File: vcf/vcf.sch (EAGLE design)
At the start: 55 parts, among them IC1 OPA4130U, IC2 OPA4130U, IC3 OPA4130U, IC4 OPA4130U, Q1 BC847ASMD, Q2 BC847ASMD, Q3 BC847ASMD, Q4 BC847ASMD, Q5 BC847ASMD, Q6 BC847ASMD

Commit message: lasdkfj
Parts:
- removed U$5: PJ301BM, dan:PJ301BM
- added AIN2, BP, LP: PJ301BM, dan:PJ301BM
- added FREQ, GAIN1, Q: 10K, dan:US-EVUF2J
- added IC5: OPA4130U, dan:OPA4130U
- added R32, R34, R36, R37, R40, R41, R42: 100k, dan:R-US_R0603
- added R33, R35, R38, R39: 1k, dan:R-US_R0603
- added R44: 10k, dan:R-US_R0603
- added X1: 2516-, dan:2516-
- C5, C7: value 1u -> (none); device dan:C-USC0603 -> dan:CPOL-USE2.5-6
- GAIN, MODAMT: value US-EVUF2J -> 10K
- R11, R16, R5: value 1k -> 10k
- R15, R29: value 1k -> 100k
- R17: value US-EVUF2J -> 100k; device dan:US-EVUF2J -> dan:R-US_R0603
- SCALE: value (none) -> 10K
- renumbered R21 to GAIN, R27 to MODAMT, R28 to SCALE, U$4 to AIN, U$6 to MIN, U$7 to MIN2
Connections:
- new net N$48: IC4D.-IN, IC4D.OUT, R35.2
- new net N$49: IC4C.-IN, IC4C.OUT, R33.2
- new net N$50: IC5B.-IN, IC5B.OUT, R38.2
- new net N$51: IC4B.-IN, R32.2, R35.1
- new net N$52: IC4B.OUT, R32.1, R42.2
- new net N$53: IC5C.-IN, IC5C.OUT, R39.2
- new net N$54: IC4B.+IN, R33.1, R34.1
- new net N$55: IC5A.+IN, R37.2, R38.1
- new net N$56: IC5A.-IN, R36.2, R39.1
- new net N$57: BP.P$1, BP.P$2, BP.P$4
- new net N$58: IC5A.OUT, R36.1
- new net N$59: IC5D.-IN, R40.2, R41.1, R42.1
- new net N$60: FREQ.S, R44.1
- new net N$61: BP.P$3, IC5D.OUT, R40.1
- new net N$62: GAIN1.A, R20.1
- net +12V: now also FREQ.E, IC5A.V+, X1-10.KL, X1-9.KL
- net -12V: now also FREQ.A, IC5A.V-, X1-1.KL, X1-2.KL
- net GND: now also AIN2.P$1, AIN2.P$2, AIN2.P$4, IC5D.+IN, LP.P$1, LP.P$2, LP.P$4, R17.2, R34.2, R37.1, X1-3.KL, X1-4.KL, X1-5.KL, X1-6.KL, X1-7.KL, X1-8.KL; no longer U$5.P$1, U$5.P$2, U$5.P$4
- net N$14: now also C5.+; no longer C5.2
- net N$2: now also IC4C.+IN
- net N$21: now also C5.-; no longer C5.1
- net N$27: now also LP.P$3, Q.A; no longer R17.A
- net N$30: now also GAIN1.E, GAIN1.S; no longer R20.1
- net N$31: now also C7.+; no longer C7.1
- net N$32: now also C7.-, Q.E, Q.S; no longer C7.2, R17.E, R17.S
- net N$33: now also AIN2.P$3; no longer U$5.P$3
- net N$36: now also R44.2
- net N$4: now also IC5B.+IN
- net N$45: now also R17.1
- net N$47: now also R41.2
- net N$5: now also IC5C.+IN
- net N$7: now also IC4D.+IN
- net N$8: now also IC1D.+IN; no longer IC1C.+IN
- net N$9: now also IC1C.+IN; no longer IC1D.+IN
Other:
- moved on the sheet: C2, C3, C4, IC1B, IC1C, IC1D, IC2D, IC3C, IC3D, IC4A, IC4B, IC4C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

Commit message: made changes to the vcf board
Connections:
- removed net N$57: BP.P$1, BP.P$2, BP.P$4
- net GND: now also BP.P$1, BP.P$2, BP.P$4, R6.1
- net N$35: now also IC2B.OUT
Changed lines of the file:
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@@
 <wire x1="20.32" y1="10.16" x2="20.32" y2="12.7" width="0.1524" layer="91"/>
 <pinref part="C6" gate="G$1" pin="2"/>
-<wire x1="20.32" y1="12.7" x2="20.32" y2="17.78" width="0.1524" layer="91"/>
+<wire x1="20.32" y1="12.7" x2="20.32" y2="15.24" width="0.1524" layer="91"/>
 <wire x1="7.62" y1="17.78" x2="7.62" y2="12.7" width="0.1524" layer="91"/>
 <wire x1="7.62" y1="12.7" x2="20.32" y2="12.7" width="0.1524" layer="91"/>
 <junction x="20.32" y="12.7"/>
+<pinref part="R6" gate="G$1" pin="1"/>
 </segment>
 <segment>
@@
 <junction x="154.94" y="203.2"/>
 <wire x1="149.86" y1="205.74" x2="154.94" y2="205.74" width="0.1524" layer="91"/>
+<junction x="154.94" y="205.74"/>
+</segment>
+<segment>
+<pinref part="BP" gate="G$1" pin="P$2"/>
+<wire x1="218.44" y1="81.28" x2="215.9" y2="81.28" width="0.1524" layer="91"/>
+<wire x1="215.9" y1="81.28" x2="215.9" y2="86.36" width="0.1524" layer="91"/>
+<pinref part="BP" gate="G$1" pin="P$4"/>
+<wire x1="215.9" y1="86.36" x2="215.9" y2="88.9" width="0.1524" layer="91"/>
+<wire x1="215.9" y1="88.9" x2="218.44" y2="88.9" width="0.1524" layer="91"/>
+<pinref part="BP" gate="G$1" pin="P$1"/>
+<wire x1="218.44" y1="86.36" x2="215.9" y2="86.36" width="0.1524" layer="91"/>
+<junction x="215.9" y="86.36"/>
+<wire x1="215.9" y1="88.9" x2="210.82" y2="88.9" width="0.1524" layer="91"/>
+<wire x1="210.82" y1="88.9" x2="210.82" y2="86.36" width="0.1524" layer="91"/>
+<junction x="215.9" y="88.9"/>
+<pinref part="GND20" gate="1" pin="GND"/>
 </segment>
 </net>
@@
 <pinref part="C7" gate="G$1" pin="-"/>
 <wire x1="86.36" y1="38.1" x2="104.14" y2="38.1" width="0.1524" layer="91"/>
+<junction x="104.14" y="38.1"/>
 </segment>
 </net>
@@
 <wire x1="-96.52" y1="12.7" x2="-96.52" y2="5.08" width="0.1524" layer="91"/>
 <junction x="-96.52" y="5.08"/>
+<junction x="-101.6" y="5.08"/>
 </segment>
 </net>
@@
 </segment>
 </net>
-<net name="N$18" class="0">
-<segment>
-<pinref part="IC2" gate="C" pin="+IN"/>
-<wire x1="-127" y1="38.1" x2="-124.46" y2="38.1" width="0.1524" layer="91"/>
-<wire x1="-124.46" y1="38.1" x2="-139.7" y2="38.1" width="0.1524" layer="91"/>
-<pinref part="AIN" gate="G$1" pin="P$3"/>
-</segment>
-</net>
 <net name="N$33" class="0">
 <segment>
@@
 <wire x1="-38.1" y1="-43.18" x2="-38.1" y2="-33.02" width="0.1524" layer="91"/>
 <junction x="-38.1" y="-33.02"/>
+<pinref part="IC2" gate="B" pin="OUT"/>
 </segment>
 </net>
@@
 </segment>
 </net>
-<net name="N$57" class="0">
-<segment>
-<pinref part="BP" gate="G$1" pin="P$2"/>
-<wire x1="218.44" y1="81.28" x2="215.9" y2="81.28" width="0.1524" layer="91"/>
-<wire x1="215.9" y1="81.28" x2="215.9" y2="86.36" width="0.1524" layer="91"/>
-<pinref part="BP" gate="G$1" pin="P$4"/>
-<wire x1="215.9" y1="86.36" x2="215.9" y2="88.9" width="0.1524" layer="91"/>
-<wire x1="215.9" y1="88.9" x2="218.44" y2="88.9" width="0.1524" layer="91"/>
-<pinref part="BP" gate="G$1" pin="P$1"/>
-<wire x1="218.44" y1="86.36" x2="215.9" y2="86.36" width="0.1524" layer="91"/>
-<junction x="215.9" y="86.36"/>
-<wire x1="215.9" y1="88.9" x2="210.82" y2="88.9" width="0.1524" layer="91"/>
-<wire x1="210.82" y1="88.9" x2="210.82" y2="83.82" width="0.1524" layer="91"/>
-<junction x="215.9" y="88.9"/>
-</segment>
-</net>
 <net name="N$60" class="0">
 <segment>
@@
 </segment>
 </net>
+<net name="N$18" class="0">
+<segment>
+<pinref part="AIN" gate="G$1" pin="P$3"/>
+<pinref part="IC2" gate="C" pin="+IN"/>
+<wire x1="-139.7" y1="38.1" x2="-124.46" y2="38.1" width="0.1524" layer="91"/>
+</segment>
+</net>

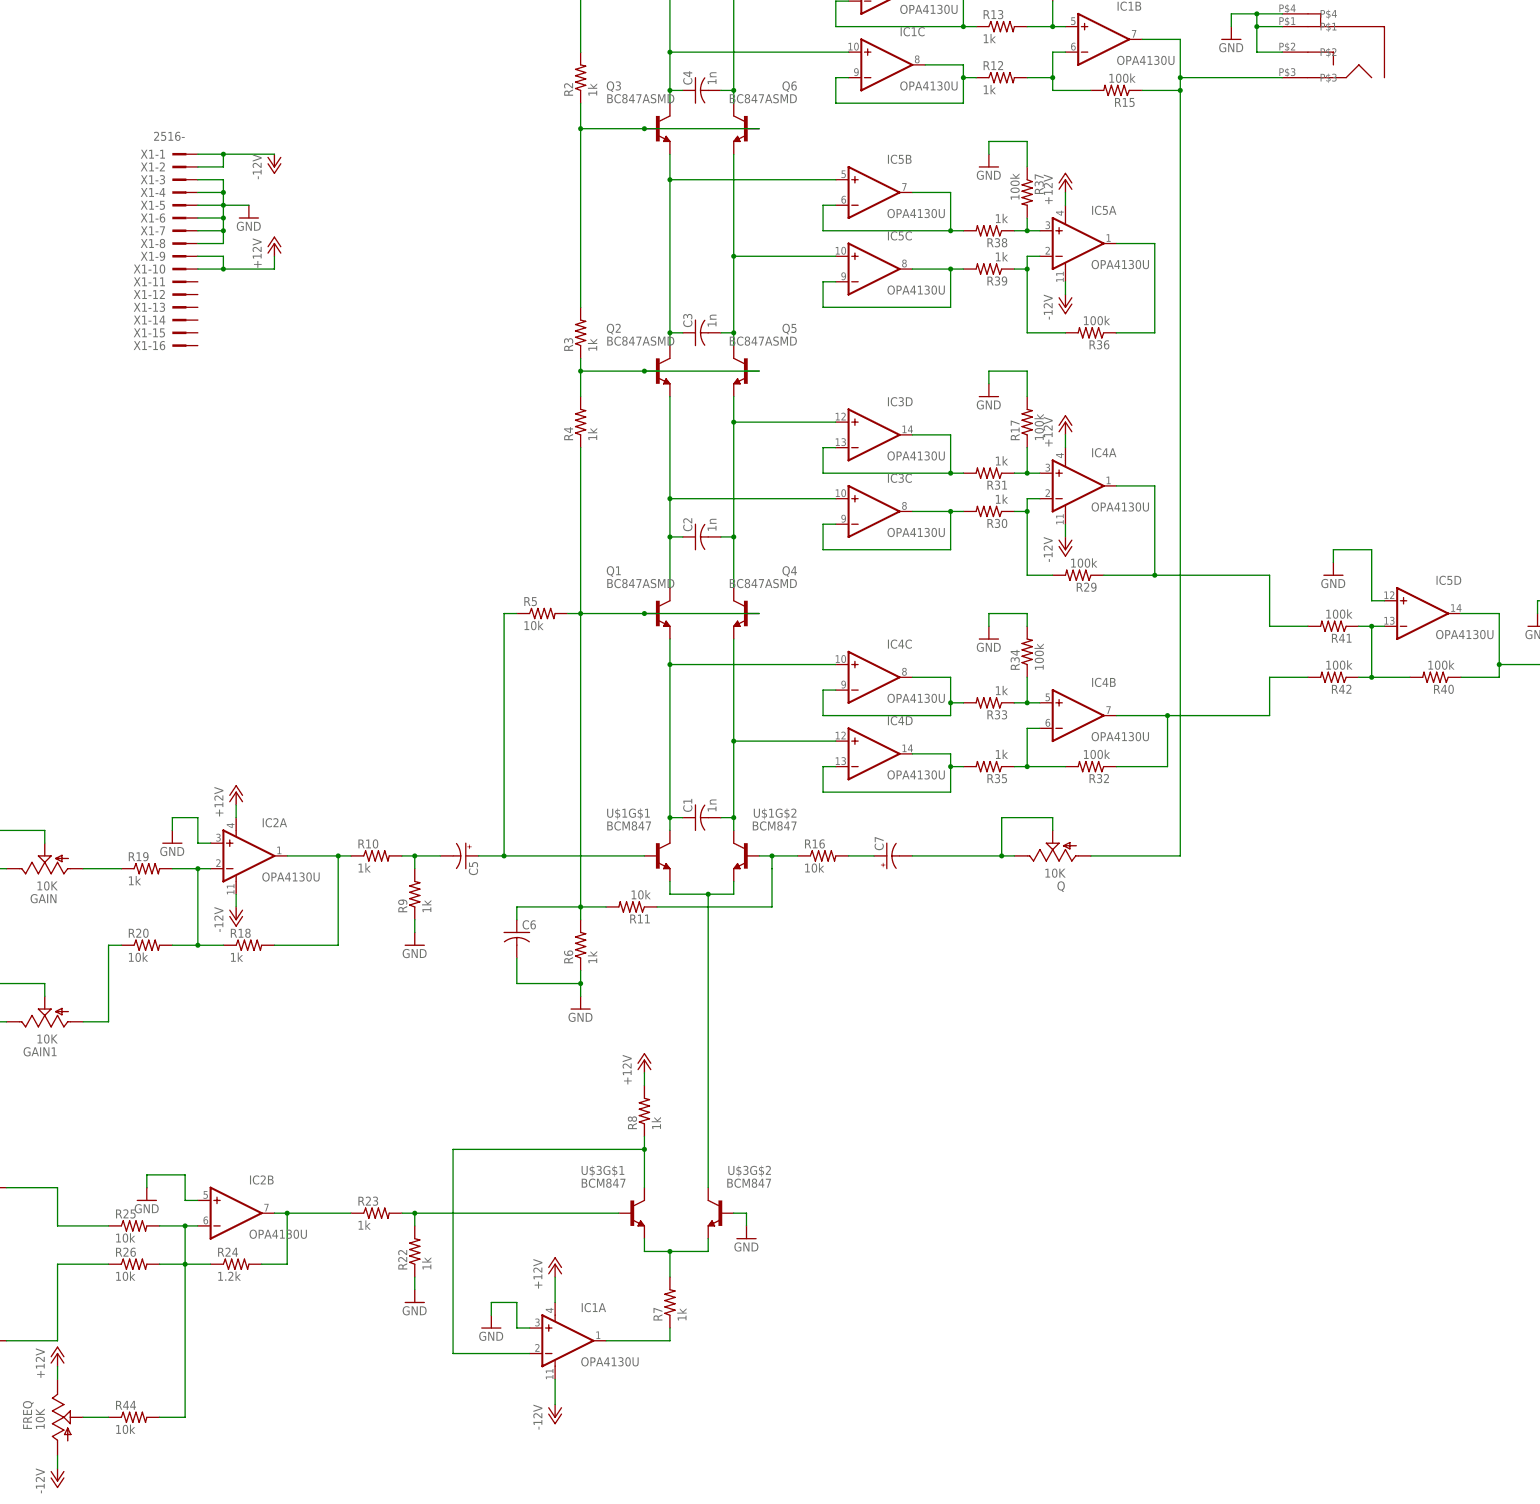
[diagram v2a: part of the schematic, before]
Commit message: changed layouts, changed vias to round.
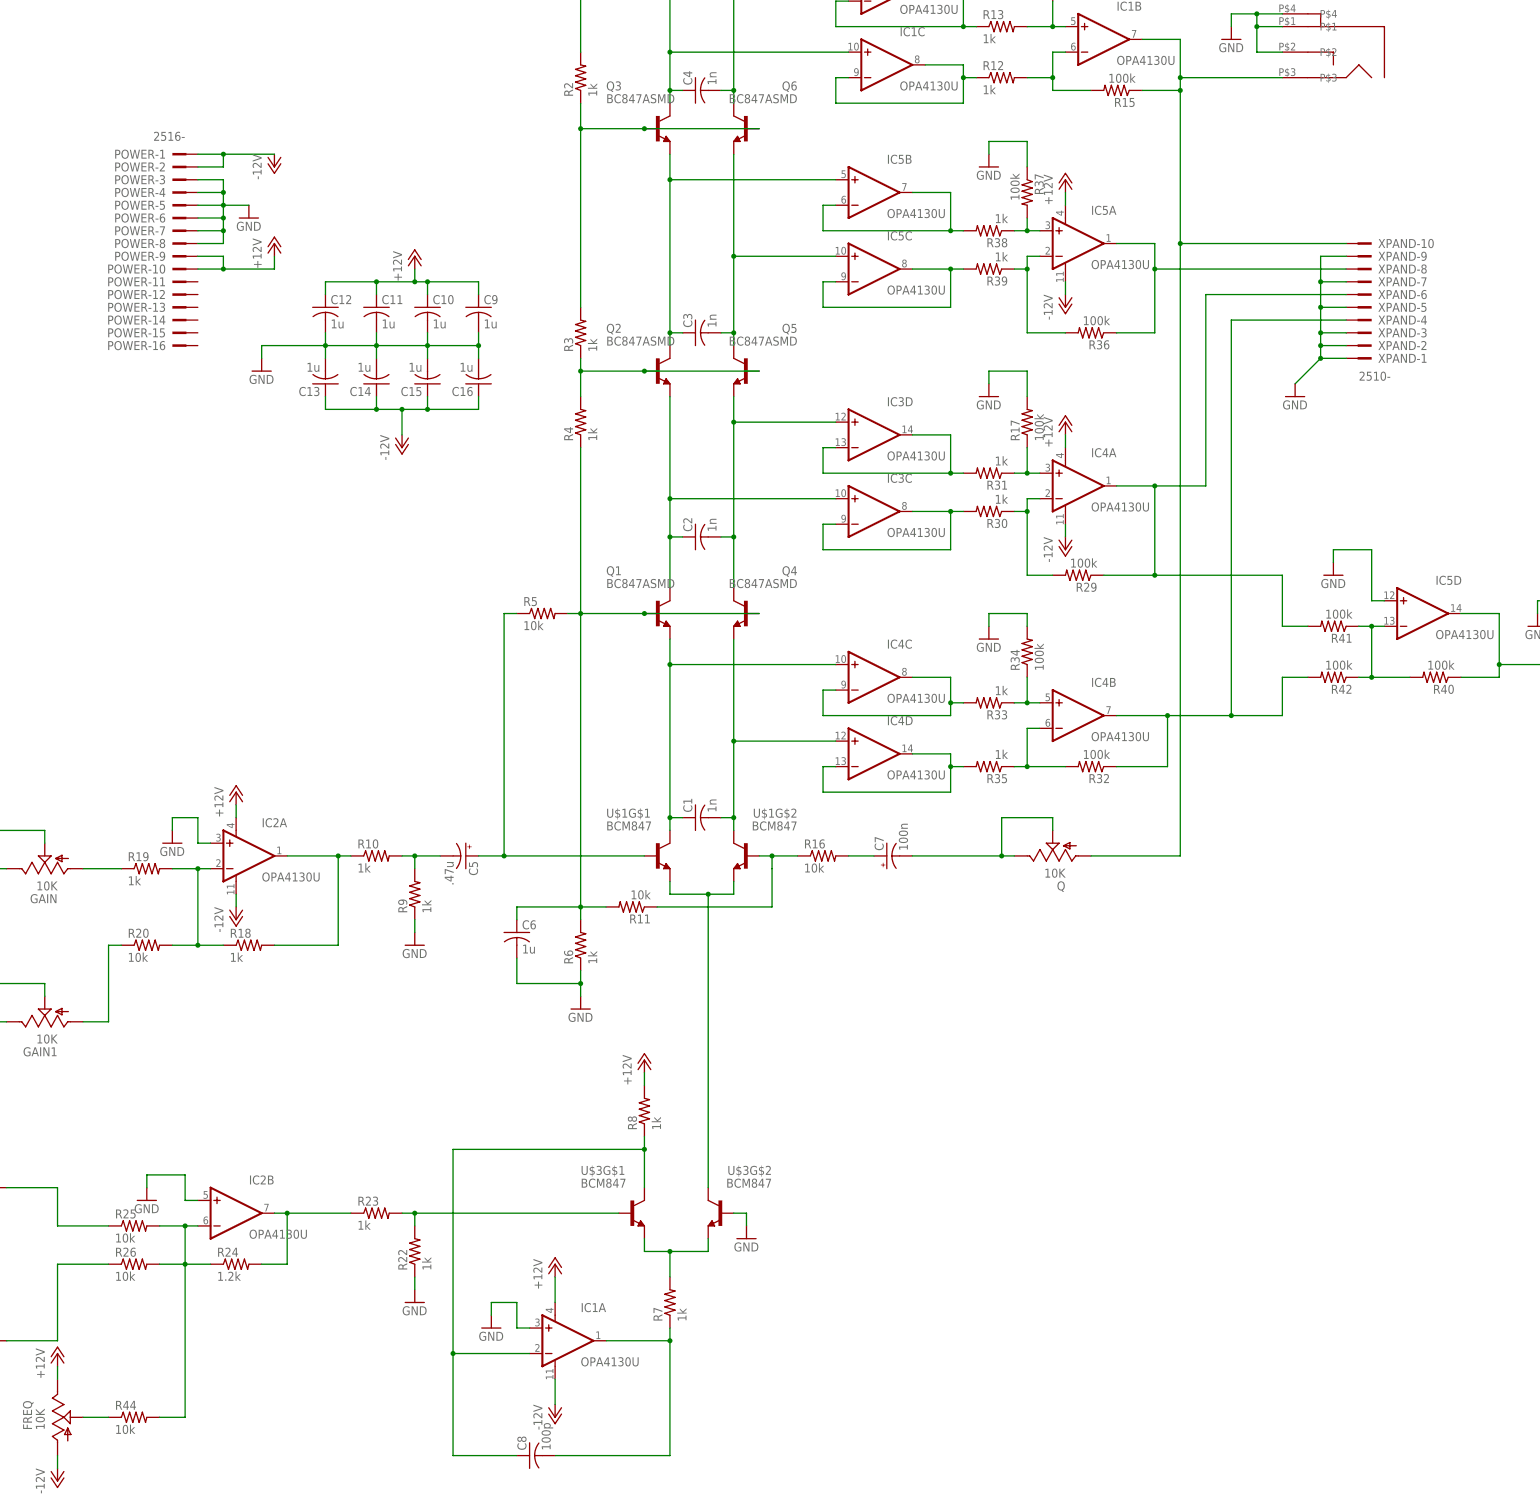
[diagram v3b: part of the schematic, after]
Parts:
- added C10, C11, C12, C13, C14, C15, C16, C9: 1u, dan:C-USC0603
- added C8: 100p, dan:C-USC0603
- added XPAND: 2510-, dan:2510-
- C5: value (none) -> .47u
- C6: value (none) -> 1u
- C7: value (none) -> 100n
- renumbered X1 to POWER
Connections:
- net +12V: now also C10.1, C11.1, C12.1, C9.1
- net -12V: now also C13.1, C14.1, C15.1, C16.1
- net GND: now also C10.2, C11.2, C12.2, C13.2, C14.2, C15.2, C16.2, C9.2, XPAND-1.KL, XPAND-2.KL, XPAND-3.KL, XPAND-5.KL, XPAND-7.KL, XPAND-9.KL
- net N$17: now also C8.2
- net N$19: now also C8.1
- net N$27: now also XPAND-10.KL
- net N$47: now also XPAND-6.KL
- net N$52: now also XPAND-4.KL
- net N$58: now also XPAND-8.KL

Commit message: changed a bunch of stuff.
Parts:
- added C17, C18, C19, C20: 1u, dan:C-USC0603
- C5: value .47u -> 4.7u
- C7: value 100n -> 4.7u
- R14, R7: value 1k -> 10k
- R15, R17, R29, R32, R34, R36, R37: value 100k -> 10k
- R20: value 10k -> 1k
- R8: value 1k -> 2Meg
- renumbered MIN2 to VPEROCT
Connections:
- removed net N$49: IC4C.-IN, IC4C.OUT, R33.2
- new net N$57: GAIN.S, R19.1
- new net N$63: GAIN.E, IC1A.-IN, IC1A.OUT
- net +12V: now also C17.1, C19.1
- net -12V: now also C18.1, C20.1
- net GND: now also C17.2, C18.2, C19.2, C20.2, GAIN.A, GAIN1.A, IC5A.+IN, IC5C.+IN, Q.E; no longer IC1A.+IN, IC2A.+IN, IC2B.+IN
- net N$15: now also IC5A.-IN; no longer IC2A.-IN
- net N$17: now also IC5D.OUT; no longer IC1A.OUT
- net N$18: now also IC1A.+IN; no longer IC2C.+IN
- net N$19: now also IC5D.-IN; no longer IC1A.-IN
- net N$2: now also IC3C.+IN; no longer IC4C.+IN
- net N$20: now also IC5A.OUT; no longer IC2A.OUT
- net N$23: now also IC2A.-IN, IC2A.OUT, R13.1; no longer IC1C.-IN, IC1C.OUT, R12.1
- net N$24: now also IC5B.+IN, R44.2; no longer IC1D.-IN, IC1D.OUT, R13.1
- net N$25: now also IC4A.-IN; no longer IC1B.-IN
- net N$26: now also IC4A.+IN; no longer IC1B.+IN
- net N$27: now also IC4A.OUT; no longer IC1B.OUT
- net N$28: now also IC2C.-IN, IC2C.OUT, R38.2; no longer GAIN.A, R19.1
- net N$29: now also IC1C.-IN, IC1C.OUT, MODAMT.E; no longer GAIN.E, GAIN.S, IC2C.-IN, IC2C.OUT
- net N$3: now also IC3B.+IN; no longer IC3C.+IN
- net N$30: now also IC1B.-IN, IC1B.OUT; no longer GAIN1.S, IC2D.-IN, IC2D.OUT
- net N$32: no longer Q.E
- net N$33: now also IC1B.+IN; no longer IC2D.+IN
- net N$35: now also IC2B.-IN, R12.1; no longer R23.1, R24.2
- net N$36: now also IC5B.-IN; no longer IC2B.-IN, R44.2
- net N$37: now also R31.2; no longer MODAMT.E
- net N$38: now also IC1D.-IN, IC1D.OUT; no longer IC3B.-IN, IC3B.OUT
- net N$39: now also IC3C.-IN, IC3C.OUT, R33.2; no longer IC3D.-IN, IC3D.OUT, R31.2
- net N$4: now also IC2C.+IN; no longer IC5B.+IN
- net N$42: now also IC2D.-IN, IC2D.OUT, R39.2; no longer IC3A.+IN, MIN.P$3
- net N$43: now also IC1D.+IN; no longer IC3B.+IN
- net N$44: now also IC3B.-IN, IC3B.OUT; no longer IC3C.-IN, IC3C.OUT
- net N$45: now also IC4C.+IN; no longer IC4A.+IN
- net N$46: now also IC4C.-IN; no longer IC4A.-IN
- net N$47: now also IC4C.OUT; no longer IC4A.OUT
- net N$48: now also IC3D.-IN, IC3D.OUT; no longer IC4D.-IN, IC4D.OUT
- net N$5: now also IC2D.+IN; no longer IC5C.+IN
- net N$50: now also IC1C.+IN, MIN.P$3; no longer IC5B.-IN, IC5B.OUT, R38.2
- net N$51: now also IC4D.-IN; no longer IC4B.-IN
- net N$52: now also IC4D.OUT; no longer IC4B.OUT
- net N$53: now also IC5B.OUT, R23.1, R24.2; no longer IC5C.-IN, IC5C.OUT, R39.2
- net N$54: now also IC4D.+IN; no longer IC4B.+IN
- net N$55: now also IC4B.+IN; no longer IC5A.+IN
- net N$56: now also IC4B.-IN; no longer IC5A.-IN
- net N$58: now also IC4B.OUT; no longer IC5A.OUT
- net N$59: now also IC5C.-IN; no longer IC5D.-IN
- net N$6: now also IC3A.+IN; no longer IC3D.+IN
- net N$61: now also IC5C.OUT; no longer IC5D.OUT
- net N$62: now also GAIN1.S; no longer GAIN1.A
- net N$7: now also IC3D.+IN; no longer IC4D.+IN
- net N$8: now also IC2A.+IN; no longer IC1D.+IN
- net N$9: now also IC2B.+IN; no longer IC1C.+IN
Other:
- note added: "Buffers have to be fet input. Probably just make these TL084"
- note added: "Make sure the buffers don't share packages with the instrumentation amps."
- note added: "coupling between IC5A and IC5D might be a conceern"
- moved on the sheet: C6, C8, FREQ, GAIN, GAIN1, IC1A, IC1B, IC1C, IC1D, IC2A, IC2B, IC2C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

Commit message: vcf, added protection and input resistors.  Added holes on corners.  fixed silkscreen.  generated viable gerbers for vcf.
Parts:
- added R21, R27, R28, R43: 1meg, dan:R-US_R0603
- added R45, R46: 1k, dan:R-US_R0603
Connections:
- new net N$49: BP.P$3, R45.1
- new net N$64: LP.P$3, R46.1
- net GND: now also R21.1, R27.1, R28.1, R43.1
- net N$18: now also R21.2
- net N$27: now also R46.2; no longer LP.P$3
- net N$33: now also R27.2
- net N$43: now also R43.2
- net N$50: now also R28.2
- net N$61: now also R45.2; no longer BP.P$3
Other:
- note added: "Double check this polarity"
